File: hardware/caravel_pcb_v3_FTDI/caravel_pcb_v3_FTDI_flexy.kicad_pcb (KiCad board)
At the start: 2 copper layers, 76.2 x 70.2 mm, 60 parts, among them J1 USB_B_Micro - 10118193-0001LF, J10 Conn_01x27_Female, J11 Conn_01x20_Female, J2 Conn_01x02_Female, J3 Conn_01x02_Female, J5 Conn_01x02_Male, J6 Conn_01x02_Male, J7 Conn_01x06_Female, J8 Conn_01x02_Male, J9 Conn_01x02_Male, SW1 SW_Push - SKQGADE010, T1 Logo, T2 Logo, U1 FT232H, U2 SN74LVC1G125DCKR, U3 SN74LVC1G125DCKR, U4 AZ1117CH-1.8TRG1, U5 AZ1117-3.3, U6 caravel_breakout, U7 W25Q32FVSS, X1 DSC6001_10MHZ, Y1 CSTNE12M0GH5L000R0

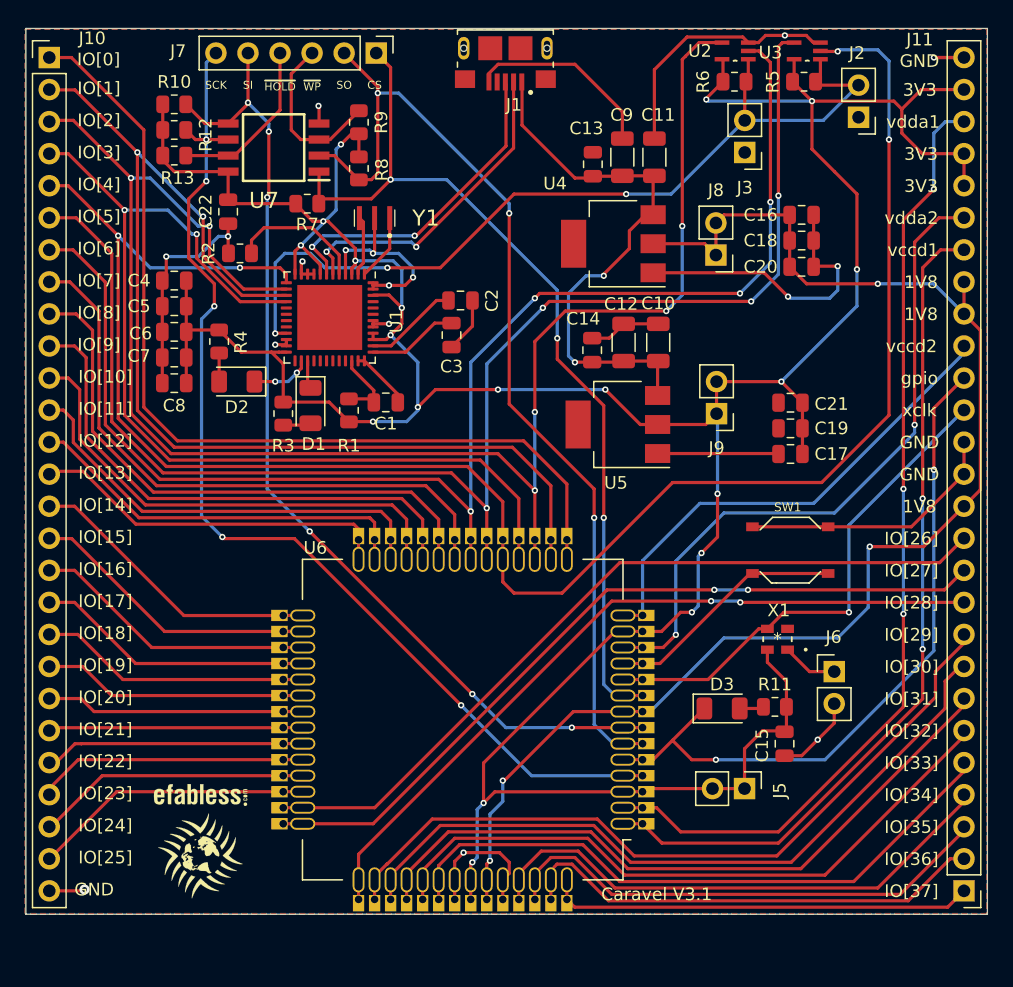
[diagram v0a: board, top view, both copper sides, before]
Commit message: add BOM of FTDI caravel board (V3.1)
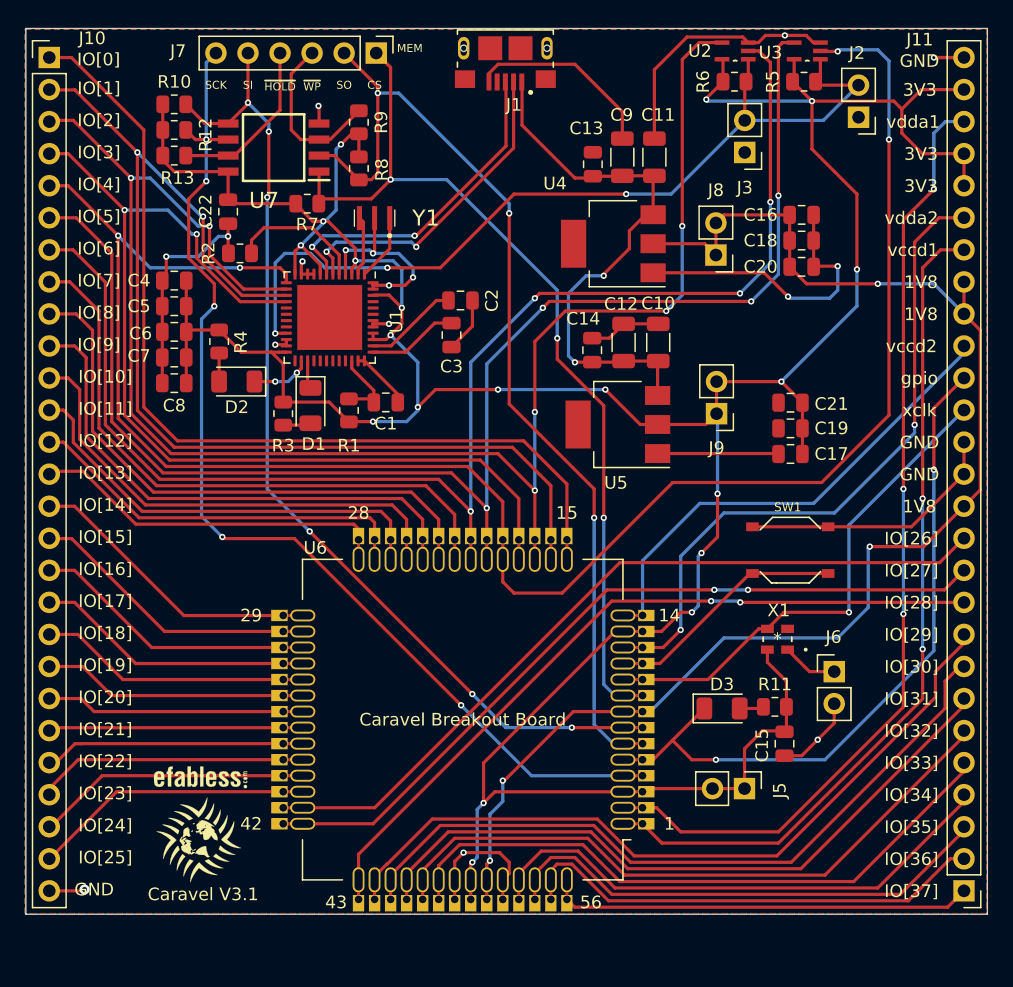
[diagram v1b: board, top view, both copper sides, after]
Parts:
- moved T2 1.40 mm to (113.8, 118.1)
- moved T1 1.28 mm to (113.7, 123.1)
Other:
- board text added: "1"
- board text added: "14"
- board text added: "15"
- board text added: "28"
- board text added: "29"
- board text added: "42"
- board text added: "43"
- board text added: "56"
- board text added: "Caravel Breakout Board"
- board text added: "MEM"
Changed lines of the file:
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@@
   )
   (footprint "Caravel_Board:ef_logo" (layer "F.Cu")
-    (at 113.792 119.507)
+    (at 113.792 118.11)
     (property "Sheetfile" "caravel_pcb_v3_FTDI_flexy.kicad_sch")
     (property "Sheetname" "")
@@
   )
   (footprint "Caravel_Board:logo" (layer "F.Cu")
-    (at 113.792 124.333)
+    (at 113.665 123.063)
     (property "Sheetfile" "caravel_pcb_v3_FTDI_flexy.kicad_sch")
     (property "Sheetname" "")
@@
     (effects (font (size 1 1) (thickness 0.15)))
   )
+  (gr_text "56" (at 144.78 128.016) (layer "F.SilkS")
+    (effects (font (size 1 1) (thickness 0.15)))
+  )
   (gr_text "IO[34]" (at 170.18 119.507) (layer "F.SilkS")
     (effects (font (size 1 1) (thickness 0.15)))
   )
+  (gr_text "42" (at 117.856 121.793) (layer "F.SilkS")
+    (effects (font (size 1 1) (thickness 0.15)))
+  )
   (gr_text "IO[7]" (at 105.791 78.74) (layer "F.SilkS")
     (effects (font (size 1 1) (thickness 0.15)))
   )
+  (gr_text "28" (at 126.365 97.155) (layer "F.SilkS")
+    (effects (font (size 1 1) (thickness 0.15)))
+  )
   (gr_text "IO[2]" (at 105.791 66.04) (layer "F.SilkS")
     (effects (font (size 1 1) (thickness 0.15)))
@@
     (effects (font (size 1 1) (thickness 0.15)))
   )
+  (gr_text "14" (at 151.003 105.283) (layer "F.SilkS")
+    (effects (font (size 1 1) (thickness 0.15)))
+  )
   (gr_text "IO[17]" (at 106.299 104.14) (layer "F.SilkS")
     (effects (font (size 1 1) (thickness 0.15)))
@@
     (effects (font (size 1 1) (thickness 0.15)))
   )
+  (gr_text "43" (at 124.587 128.016) (layer "F.SilkS")
+    (effects (font (size 1 1) (thickness 0.15)))
+  )
   (gr_text "IO[10]" (at 106.299 86.36) (layer "F.SilkS")
     (effects (font (size 1 1) (thickness 0.15)))
@@
     (effects (font (size 1 1) (thickness 0.15)))
   )
+  (gr_text "29" (at 117.856 105.283) (layer "F.SilkS")
+    (effects (font (size 1 1) (thickness 0.15)))
+  )
   (gr_text "IO[8]" (at 105.791 81.28) (layer "F.SilkS")
     (effects (font (size 1 1) (thickness 0.15)))
@@
     (effects (font (size 1 1) (thickness 0.15)))
   )
+  (gr_text "15" (at 142.875 97.155) (layer "F.SilkS")
+    (effects (font (size 1 1) (thickness 0.15)))
+  )
   (gr_text "~{WP}" (at 122.682 63.373) (layer "F.SilkS")
     (effects (font (size 0.635 0.635) (thickness 0.15)))
@@
     (effects (font (size 1 1) (thickness 0.15)))
   )
+  (gr_text "MEM\n" (at 130.429 60.325) (layer "F.SilkS")
+    (effects (font (size 0.635 0.635) (thickness 0.15)))
+  )
   (gr_text "GND" (at 105.41 127) (layer "F.SilkS")
     (effects (font (size 1 1) (thickness 0.15)))
@@
     (effects (font (size 1 1) (thickness 0.15)))
   )
-  (gr_text "Caravel V3.1" (at 149.987 127.381) (layer "F.SilkS")
+  (gr_text "Caravel V3.1" (at 114.046 127.381) (layer "F.SilkS")
     (effects (font (size 1 1) (thickness 0.25)))
   )
@@
     (effects (font (size 1 1) (thickness 0.15)))
   )
+  (gr_text "1\n" (at 151.003 121.793) (layer "F.SilkS")
+    (effects (font (size 1 1) (thickness 0.15)))
+  )
   (gr_text "IO[28]" (at 170.18 104.267) (layer "F.SilkS")
     (effects (font (size 1 1) (thickness 0.15)))
@@
     (effects (font (size 1 1) (thickness 0.15)))
   )
+  (gr_text "Caravel Breakout Board" (at 134.62 113.538) (layer "F.SilkS")
+    (effects (font (size 1 1) (thickness 0.25)))
+  )
   (dimension (type aligned) (layer "Dwgs.User")
     (pts (xy 176.2 128.956) (xy 100 128.956))
@@
   (via (at 171.069 107.95) (size 0.5) (drill 0.25) (layers "F.Cu" "B.Cu") (net 21))
   (segment (start 171.069 107.95) (end 171.069 96.012) (width 0.254) (layer "B.Cu") (net 21))
+  (segment (start 150.502 107.816) (end 148.87 107.816) (width 0.254) (layer "F.Cu") (net 22))
   (segment (start 172.3644 73.7616) (end 174.3456 73.7616) (width 0.254) (layer "F.Cu") (net 22))
+  (segment (start 151.892 106.426) (end 150.502 107.816) (width 0.254) (layer "F.Cu") (net 22))
   (segment (start 170.434 90.17) (end 170.434 75.692) (width 0.254) (layer "F.Cu") (net 22))
-  (segment (start 151.511 106.807) (end 150.502 107.816) (width 0.254) (layer "F.Cu") (net 22))
-  (segment (start 150.502 107.816) (end 148.87 107.816) (width 0.254) (layer "F.Cu") (net 22))
   (segment (start 170.434 75.692) (end 172.3644 73.7616) (width 0.254) (layer "F.Cu") (net 22))
   (segment (start 148.87 107.816) (end 147.32 107.816) (width 0.254) (layer "F.Cu") (net 22))
   (via (at 170.434 90.17) (size 0.5) (drill 0.25) (layers "F.Cu" "B.Cu") (net 22))
-  (via (at 151.511 106.807) (size 0.5) (drill 0.25) (layers "F.Cu" "B.Cu") (net 22))
+  (via (at 151.892 106.426) (size 0.5) (drill 0.25) (layers "F.Cu" "B.Cu") (net 22))
+  (segment (start 151.892 100.584) (end 155.321 97.155) (width 0.254) (layer "B.Cu") (net 22))
   (segment (start 155.321 97.155) (end 164.084 97.155) (width 0.254) (layer "B.Cu") (net 22))
-  (segment (start 164.084 97.155) (end 170.434 90.805) (width 0.254) (layer "B.Cu") (net 22))
-  (segment (start 151.511 100.965) (end 155.321 97.155) (width 0.254) (layer "B.Cu") (net 22))
+  (segment (start 151.892 106.426) (end 151.892 100.584) (width 0.254) (layer "B.Cu") (net 22))
   (segment (start 170.434 90.805) (end 170.434 90.17) (width 0.254) (layer "B.Cu") (net 22))
-  (segment (start 151.511 106.807) (end 151.511 100.965) (width 0.254) (layer "B.Cu") (net 22))
+  (segment (start 164.084 97.155) (end 170.434 90.805) (width 0.254) (layer "B.Cu") (net 22))
   (segment (start 159.639 122.428) (end 151.892 122.428) (width 0.254) (layer "F.Cu") (net 23))
   (segment (start 151.892 122.428) (end 149.98 120.516) (width 0.254) (layer "F.Cu") (net 23))

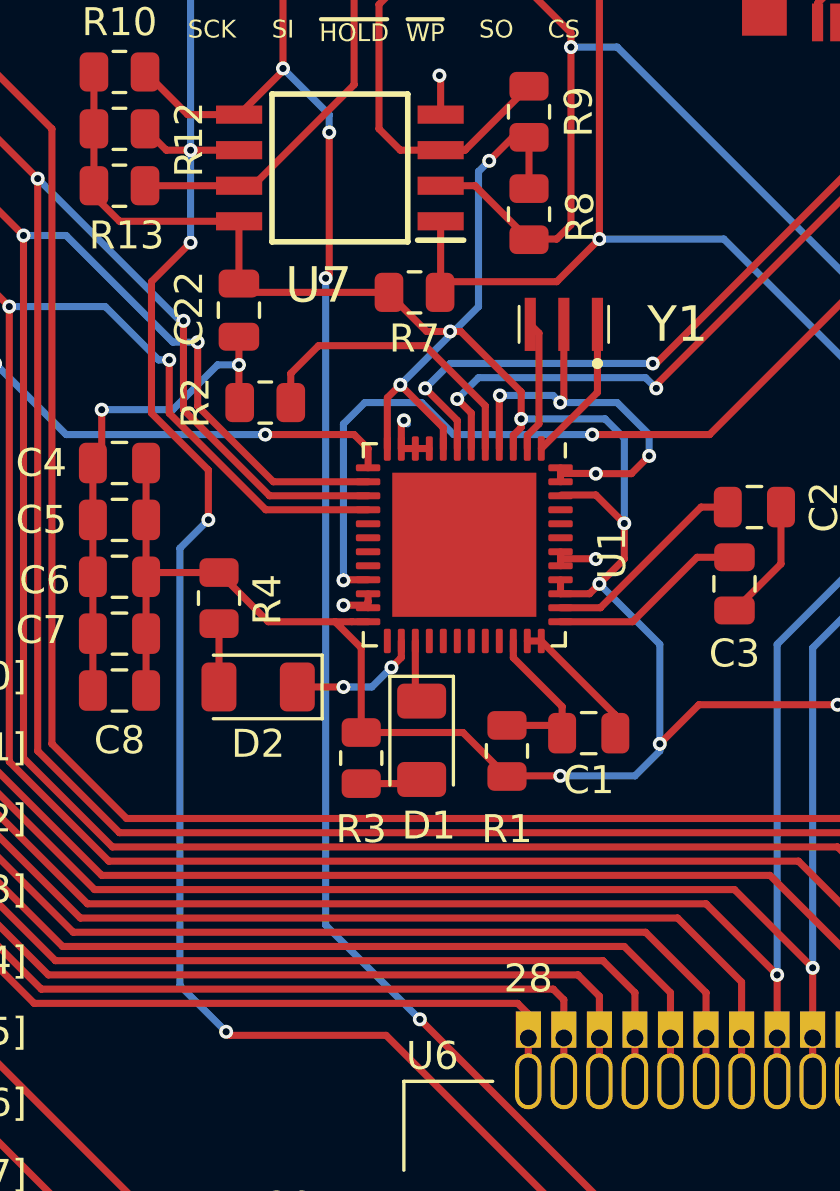
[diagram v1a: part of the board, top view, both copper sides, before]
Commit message: update FTDI footprint
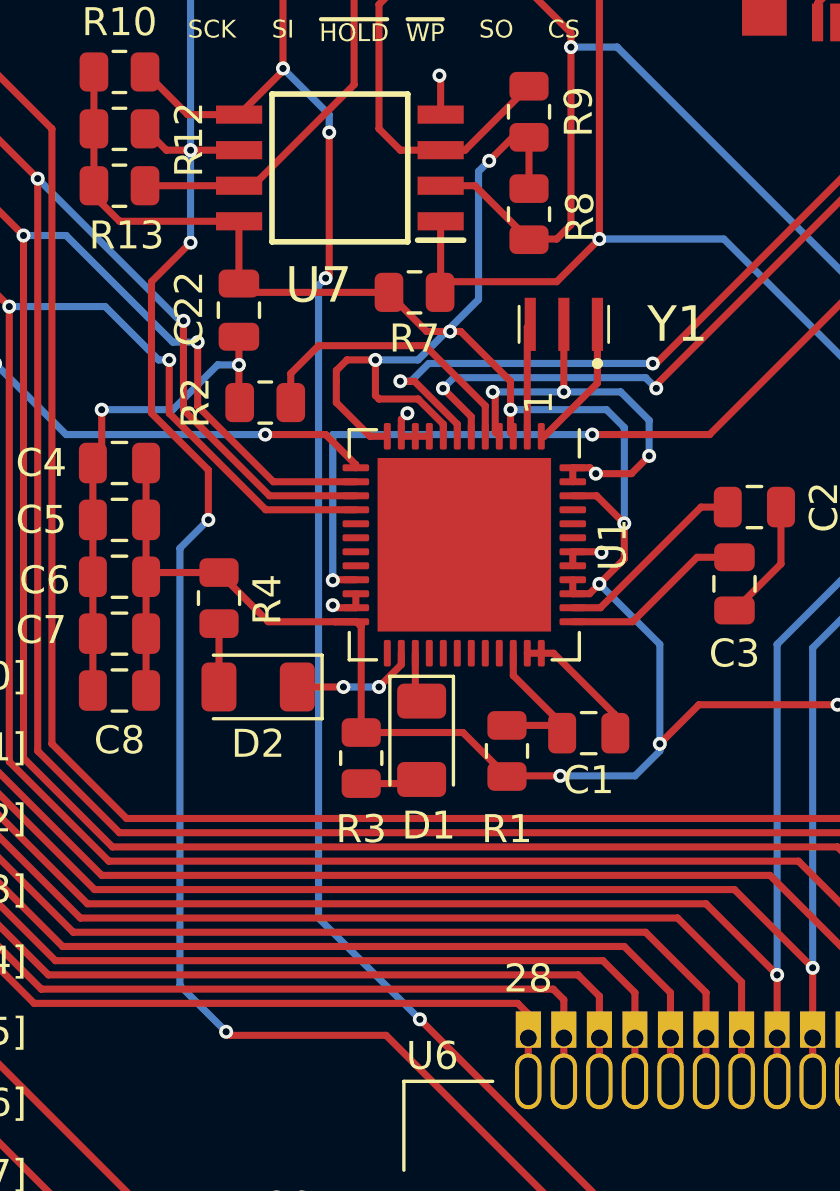
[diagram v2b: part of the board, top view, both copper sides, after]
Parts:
- U1: footprint Package_DFN_QFN:QFN-48-1EP_7x7mm_P0.5mm_EP5.15x5.15mm -> Package_DFN_QFN:QFN-48-1EP_8x8mm_P0.5mm_EP6.2x6.2mm
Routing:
- net vdda: track 288.2 -> 292.0 mm
- net FTDI_D+: track 26.2 -> 27.4 mm
- net GND: track 169.9 -> 168.9 mm
- net UART_EN: track 69.5 -> 68.6 mm
- net USB_SCK_TXD: track 147.2 -> 146.4 mm
- net Net-(U1-Pad2): track 4.74 -> 4.02 mm
- net FTDI_D-: track 25.8 -> 26.3 mm

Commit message: add gerber files
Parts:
- U1: footprint Package_DFN_QFN:QFN-48-1EP_8x8mm_P0.5mm_EP6.2x6.2mm -> FT232HQ-REEL:QFN50P800X800X90-49N

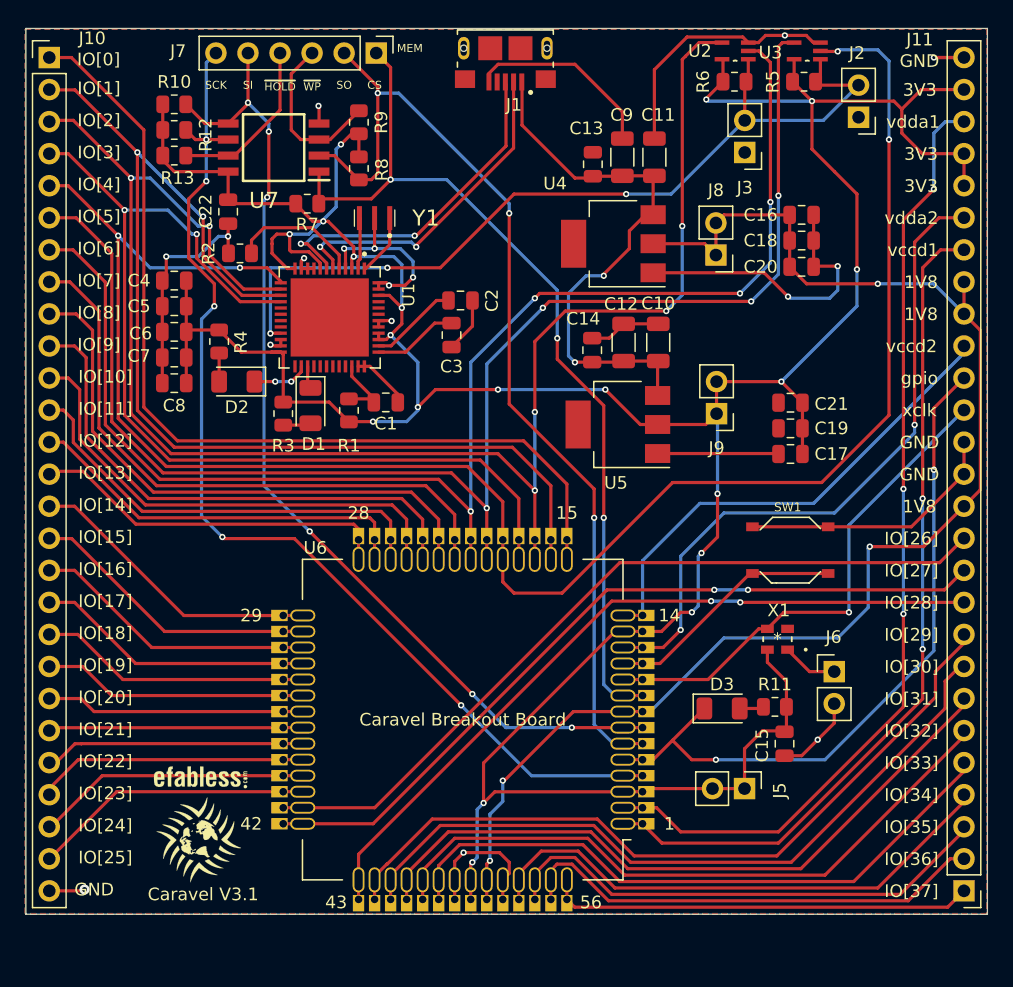
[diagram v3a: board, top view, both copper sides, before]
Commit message: fix caravel breakout pin mismatch
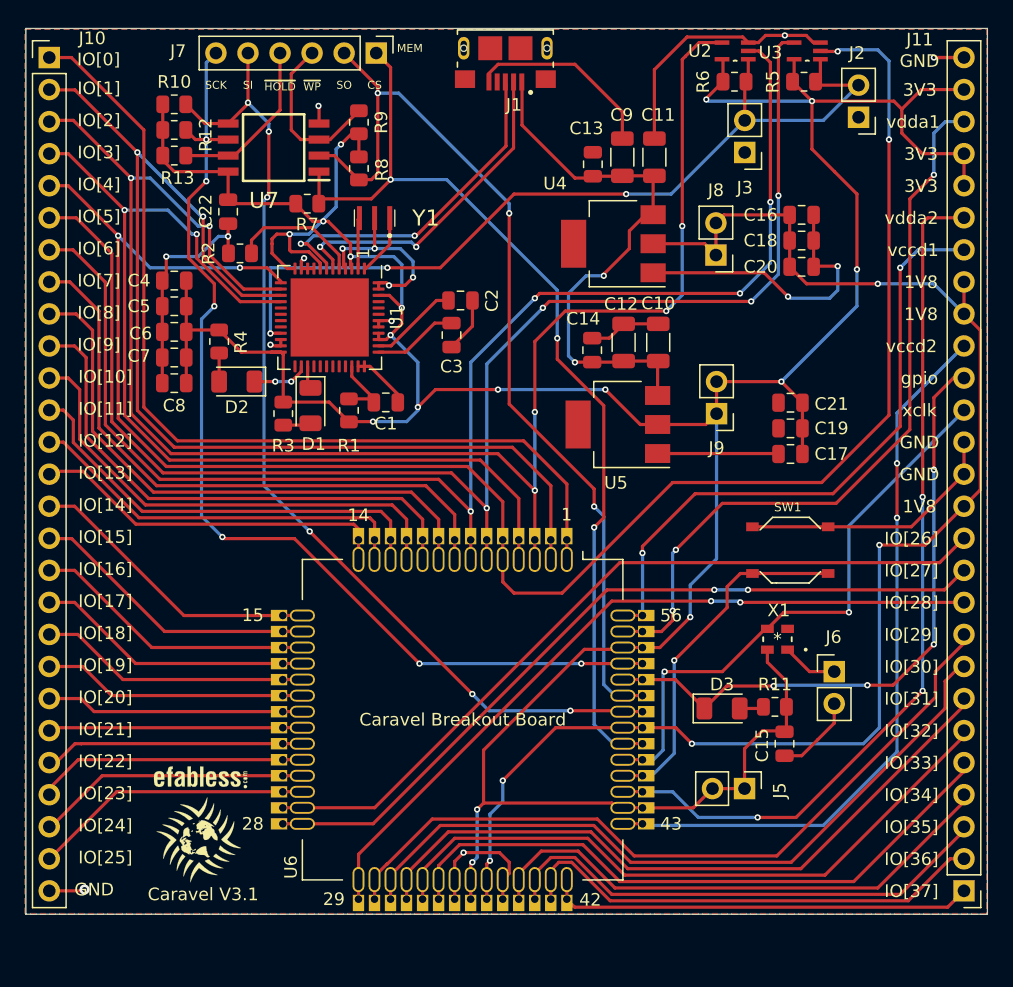
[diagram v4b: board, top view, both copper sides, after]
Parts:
- U1: footprint FT232HQ-REEL:QFN50P800X800X90-49N -> Package_DFN_QFN:QFN-48-1EP_8x8mm_P0.5mm_EP6.2x6.2mm
- turned U6 to 90 degrees
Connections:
- U6 pad 1: vccd1 -> mprj_io[0]
- U6 pad 10: xclk -> mprj_io[9]
- U6 pad 11: ~{RST} -> mprj_io[10]
- U6 pad 12: vdda2 -> mprj_io[11]
- U6 pad 13: vdda -> mprj_io[12]
- U6 pad 14: vccd2 -> mprj_io[13]
- U6 pad 15: mprj_io[0] -> mprj_io[14]
- U6 pad 16: USB_SI -> mprj_io[15]
- U6 pad 17: USB_SO_RXD -> mprj_io[16]
- U6 pad 18: USB_CS1 -> mprj_io[17]
- U6 pad 19: USB_SCK_TXD -> mprj_io[18]
- U6 pad 2: vdda1 -> USB_SI
- U6 pad 20: mprj_io[5]_ser_rx -> mprj_io[19]
- U6 pad 21: mprj_io[6]_ser_tx -> mprj_io[20]
- U6 pad 22: mprj_io[7] -> mprj_io[21]
- U6 pad 23: mprj_io[8] -> mprj_io[22]
- U6 pad 24: mprj_io[9] -> mprj_io[23]
- U6 pad 25: mprj_io[10] -> mprj_io[24]
- U6 pad 26: mprj_io[11] -> mprj_io[25]
- U6 pad 27: mprj_io[12] -> mprj_io[26]
- U6 pad 28: mprj_io[13] -> mprj_io[27]
- U6 pad 29: mprj_io[14] -> mprj_io[28]
- U6 pad 3: vdda -> USB_SO_RXD
- U6 pad 30: mprj_io[15] -> mprj_io[29]
- U6 pad 31: mprj_io[16] -> mprj_io[30]
- U6 pad 32: mprj_io[17] -> mprj_io[31]
- U6 pad 33: mprj_io[18] -> mprj_io[32]
- U6 pad 34: mprj_io[19] -> mprj_io[33]
- U6 pad 35: mprj_io[20] -> GND
- U6 pad 36: mprj_io[21] -> vdda
- U6 pad 37: mprj_io[22] -> vccd
- U6 pad 38: mprj_io[23] -> GND
- U6 pad 39: mprj_io[24] -> mprj_io[34]
- U6 pad 4: Caravel_SCK -> USB_CS1
- U6 pad 40: mprj_io[25] -> mprj_io[35]
- U6 pad 41: mprj_io[26] -> mprj_io[36]
- U6 pad 42: mprj_io[27] -> mprj_io[37]
- U6 pad 43: mprj_io[28] -> vccd2
- U6 pad 44: mprj_io[29] -> vdda
- U6 pad 45: mprj_io[30] -> vdda2
- U6 pad 46: mprj_io[31] -> ~{RST}
- U6 pad 47: mprj_io[32] -> xclk
- U6 pad 48: mprj_io[33] -> Caravel_CSB
- U6 pad 49: GND -> vccd
- U6 pad 5: gpio -> USB_SCK_TXD
- U6 pad 50: vdda -> Caravel_D0
- U6 pad 51: vccd -> Caravel_D1
- U6 pad 52: GND -> gpio
- U6 pad 53: mprj_io[34] -> Caravel_SCK
- U6 pad 54: mprj_io[35] -> vdda
- U6 pad 55: mprj_io[36] -> vdda1
- U6 pad 56: mprj_io[37] -> vccd1
- U6 pad 6: Caravel_D1 -> mprj_io[5]_ser_rx
- U6 pad 7: Caravel_D0 -> mprj_io[6]_ser_tx
- U6 pad 8: vccd -> mprj_io[7]
- U6 pad 9: Caravel_CSB -> mprj_io[8]
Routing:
- net vccd2: track 38.7 -> 58.6 mm, vias 0 -> 2
- net vccd1: track 67.1 -> 49.9 mm
- net vdda1: track 76.4 -> 59.5 mm
- net vdda2: track 53.4 -> 69.3 mm, vias 2 -> 3
- net ~{RST}: track 19.2 -> 28.3 mm, vias 0 -> 1
- net vccd: track 110.6 -> 117.4 mm, vias 4 -> 5
- net xclk: track 39.9 -> 46.1 mm, vias 1 -> 2
- net gpio: track 55.7 -> 50.3 mm, vias 2 -> 4
- net Caravel_CSB: track 72.6 -> 77.1 mm
- net Caravel_D1: track 78.9 -> 75.0 mm
- net Caravel_SCK: track 86.0 -> 82.3 mm, vias 5 -> 6
- net vdda: track 291.8 -> 292.6 mm, vias 19 -> 17
- net Caravel_D0: track 79.4 -> 78.7 mm
- net GND: track 168.6 -> 168.9 mm, vias 17 -> 16
